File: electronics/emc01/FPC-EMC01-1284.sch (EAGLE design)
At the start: 74 parts, among them J1 USB-MINIB-5PIN, J11 CONN-RECT-16PIN-2ROW, J12 CONN-RECT-16PIN-2ROW, J13 CONN-RECT-16PIN-2ROW, J14 CONN-RECT-16PIN-2ROW, J15 DNP, J16 ICSP, J2 CONN-MOLEX-MICROFIT-6PIN, J3 DNP, J4A MOT-X, J5A MOT-Y, J6A MOT-Z, J7A CONN-RECT-3PINJST_PH_2MM, J8A CONN-RECT-3PINJST_PH_2MM, J9A CONN-RECT-3PINJST_PH_2MM, Q2 2N7002PW, U1 IC-ATMEGA1284P-AU, U2 FT231XS, X1 16Mhz

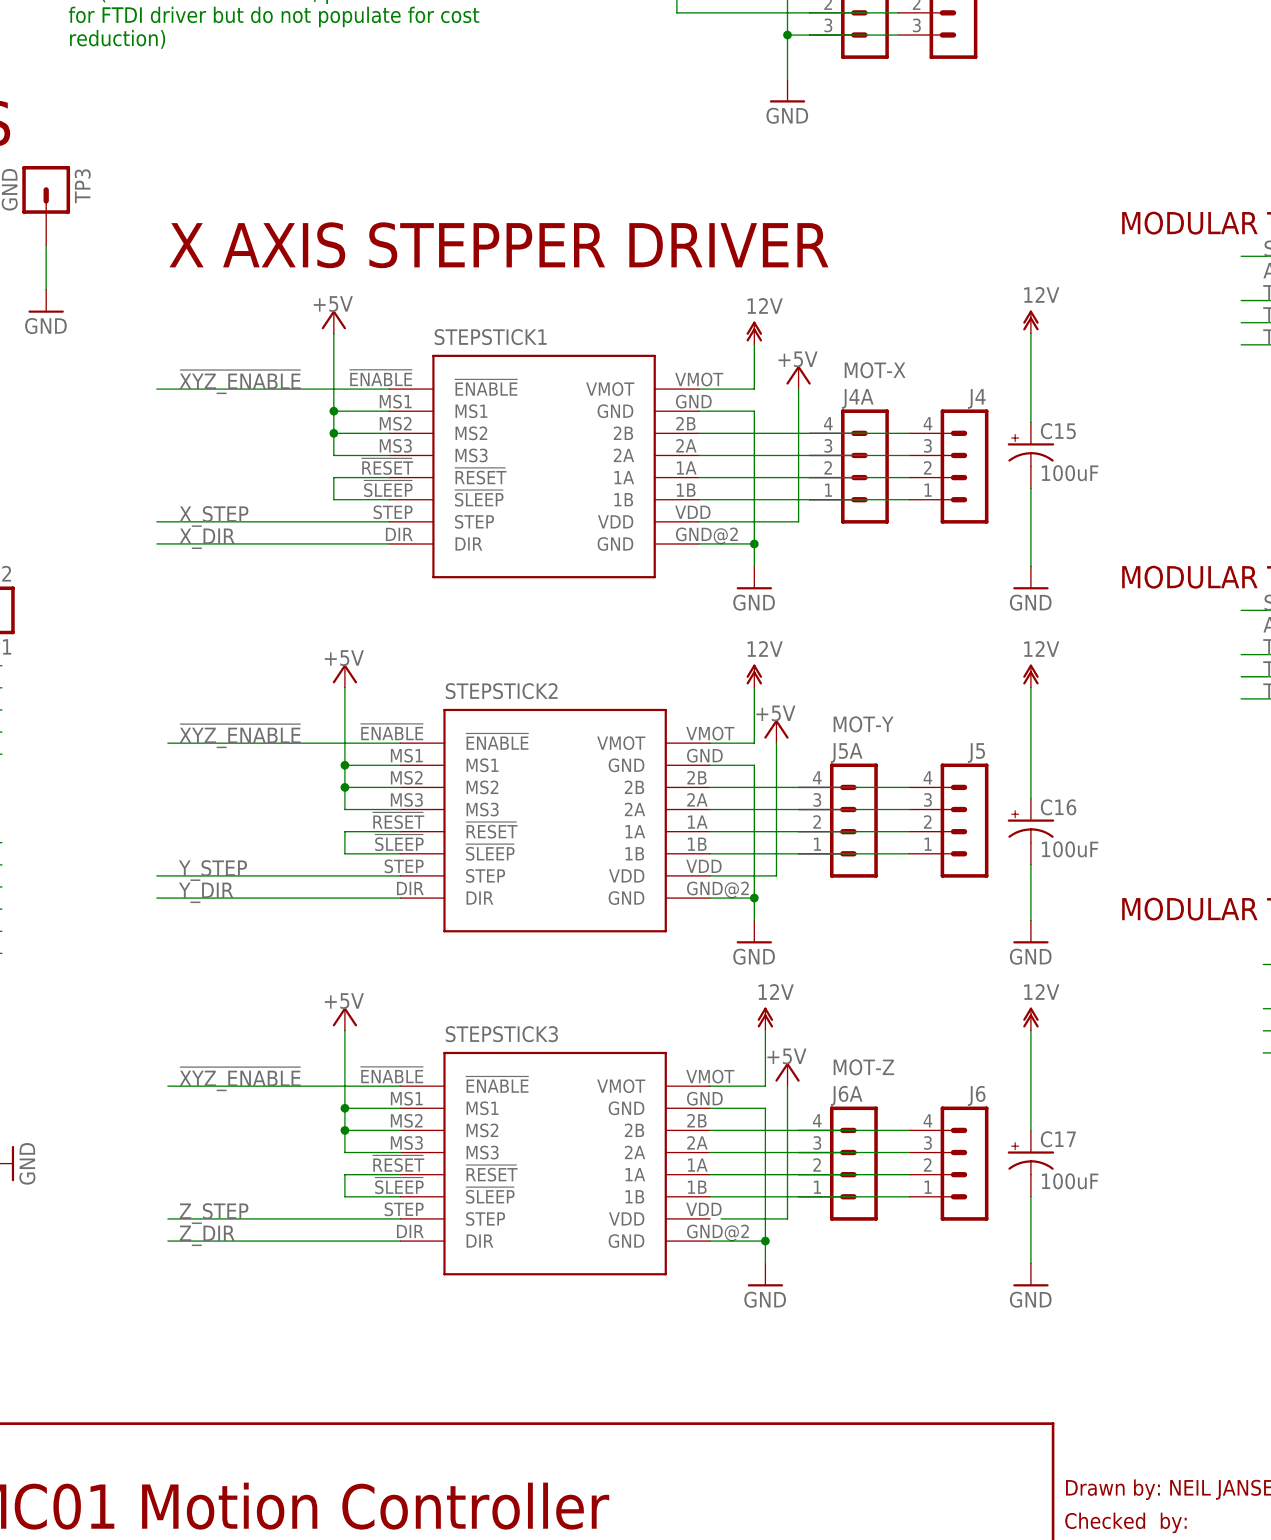
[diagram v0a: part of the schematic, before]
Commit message: Forgot some labels
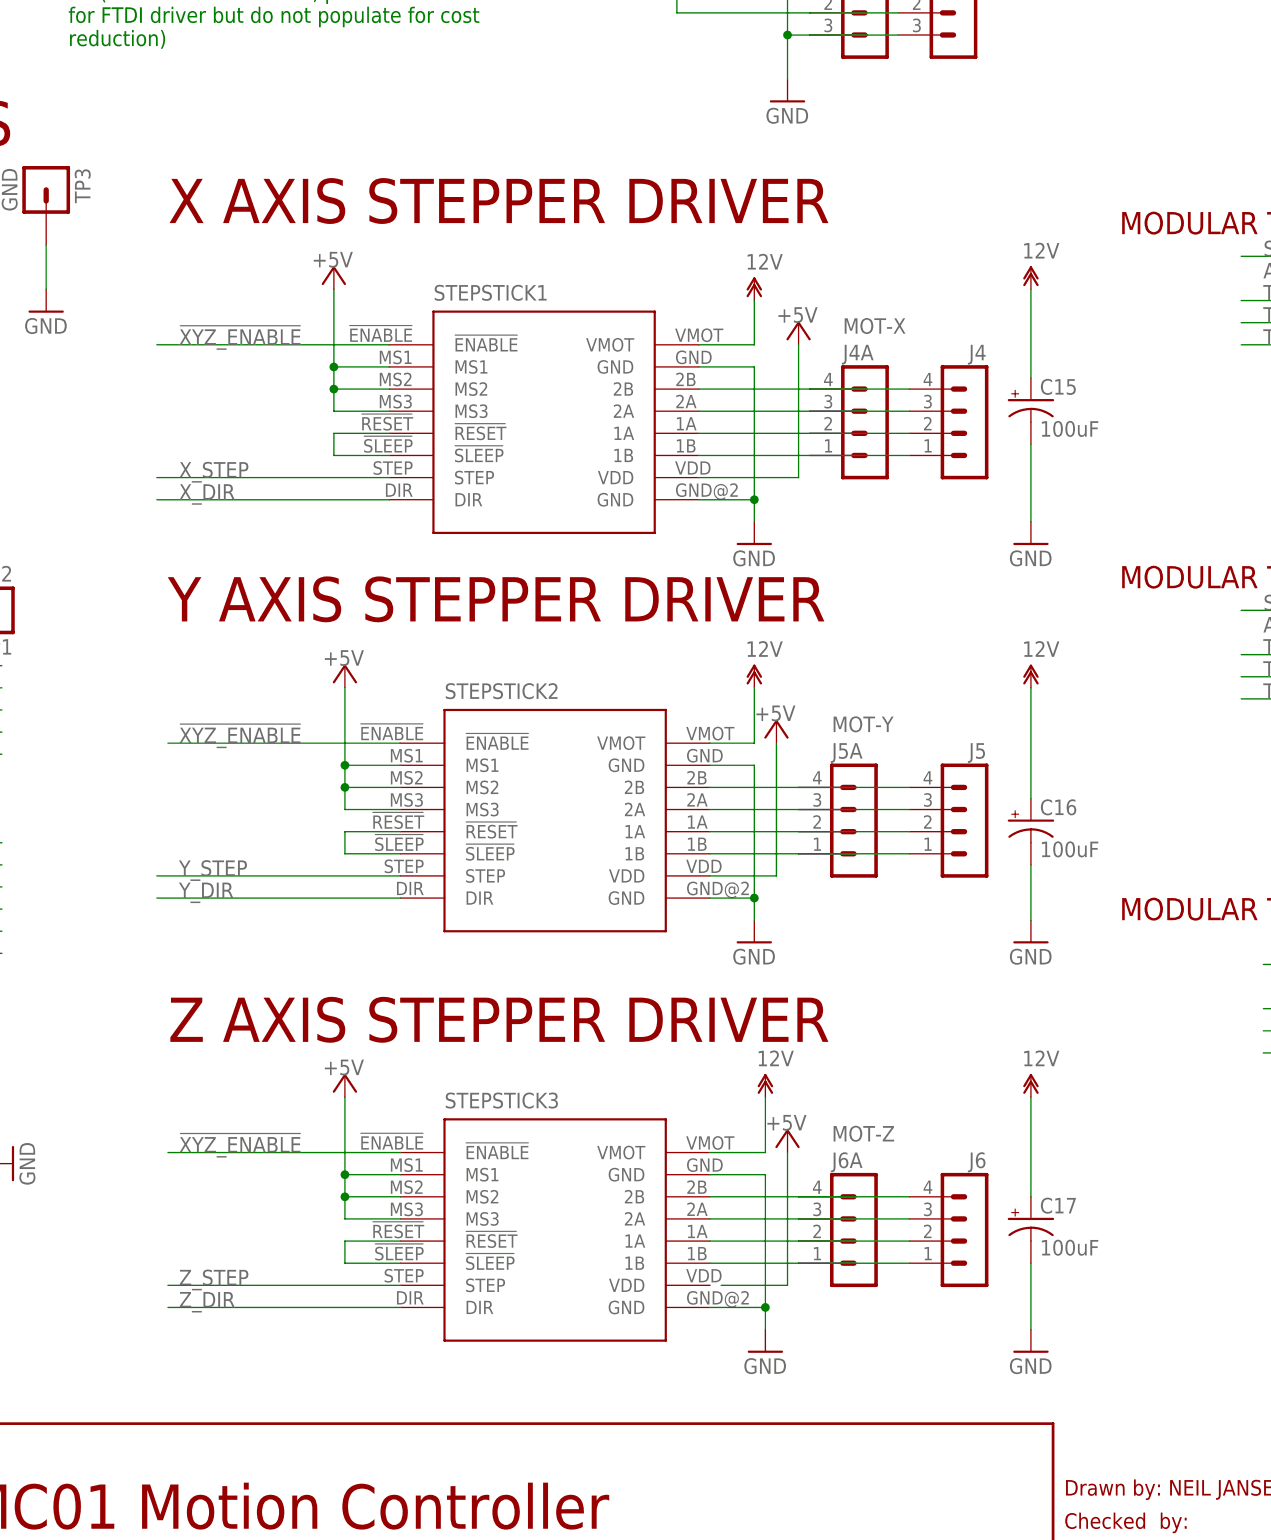
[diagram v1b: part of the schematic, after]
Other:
- note added: "Y AXIS STEPPER DRIVER"
- note added: "Z AXIS STEPPER DRIVER"
- moved on the sheet: C15, C17, J4, J4A, J6, J6A, STEPSTICK1, STEPSTICK3

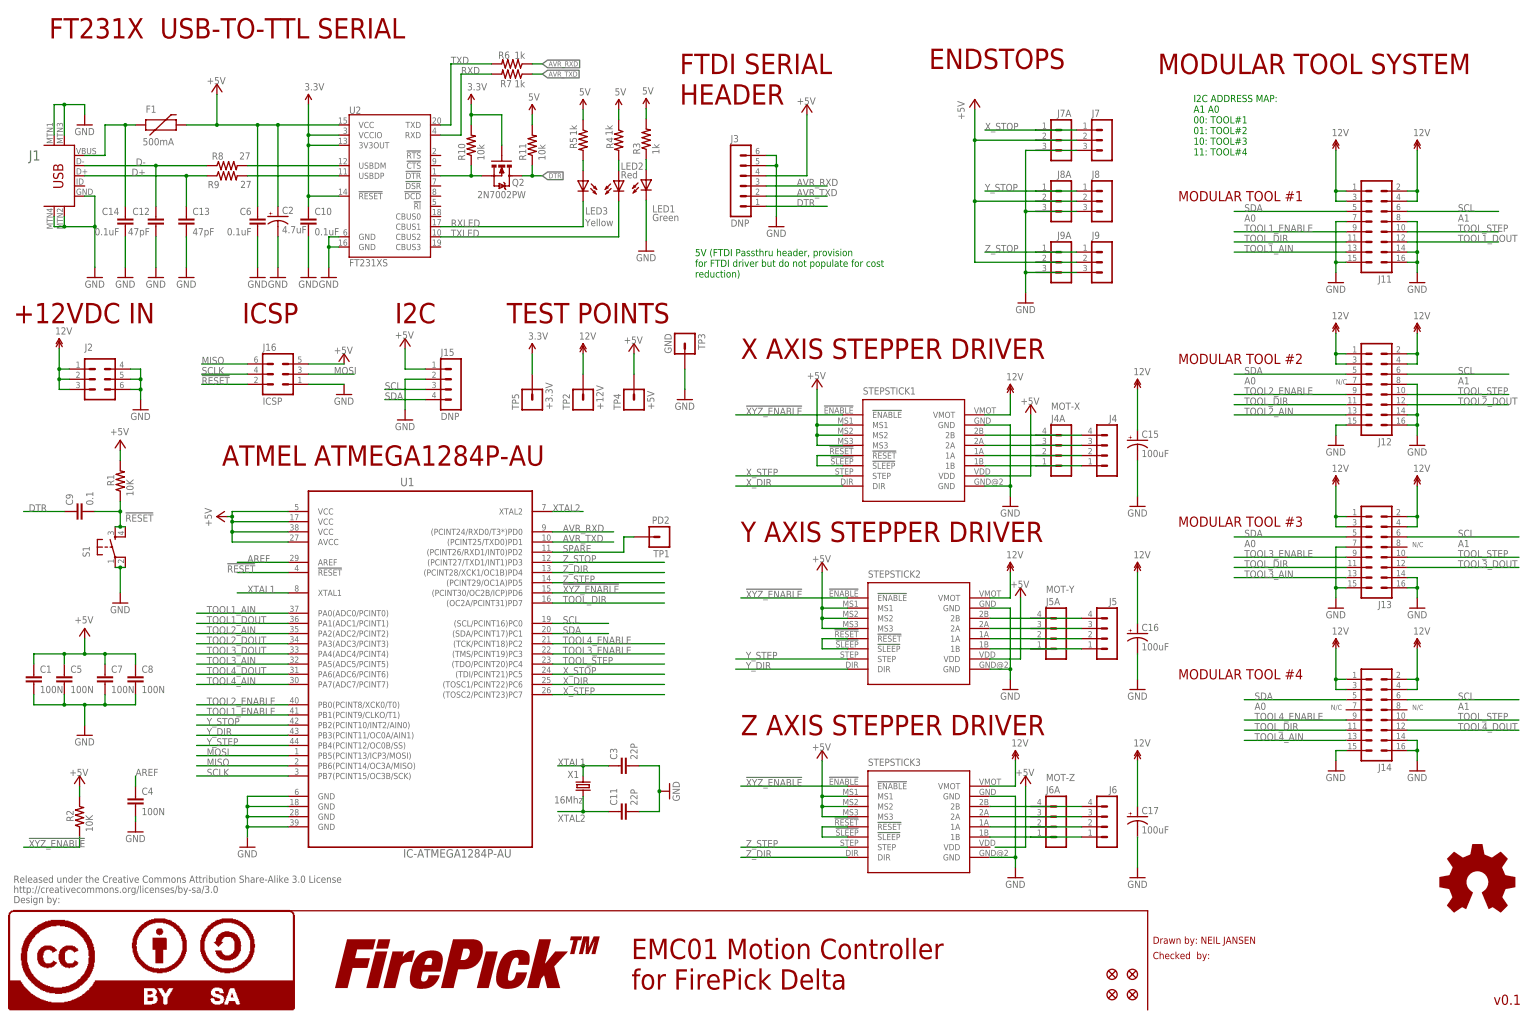
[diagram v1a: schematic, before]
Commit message: Fixed minor issues and changed modular tool connector pinout to allow better routing of GND and +12V planes
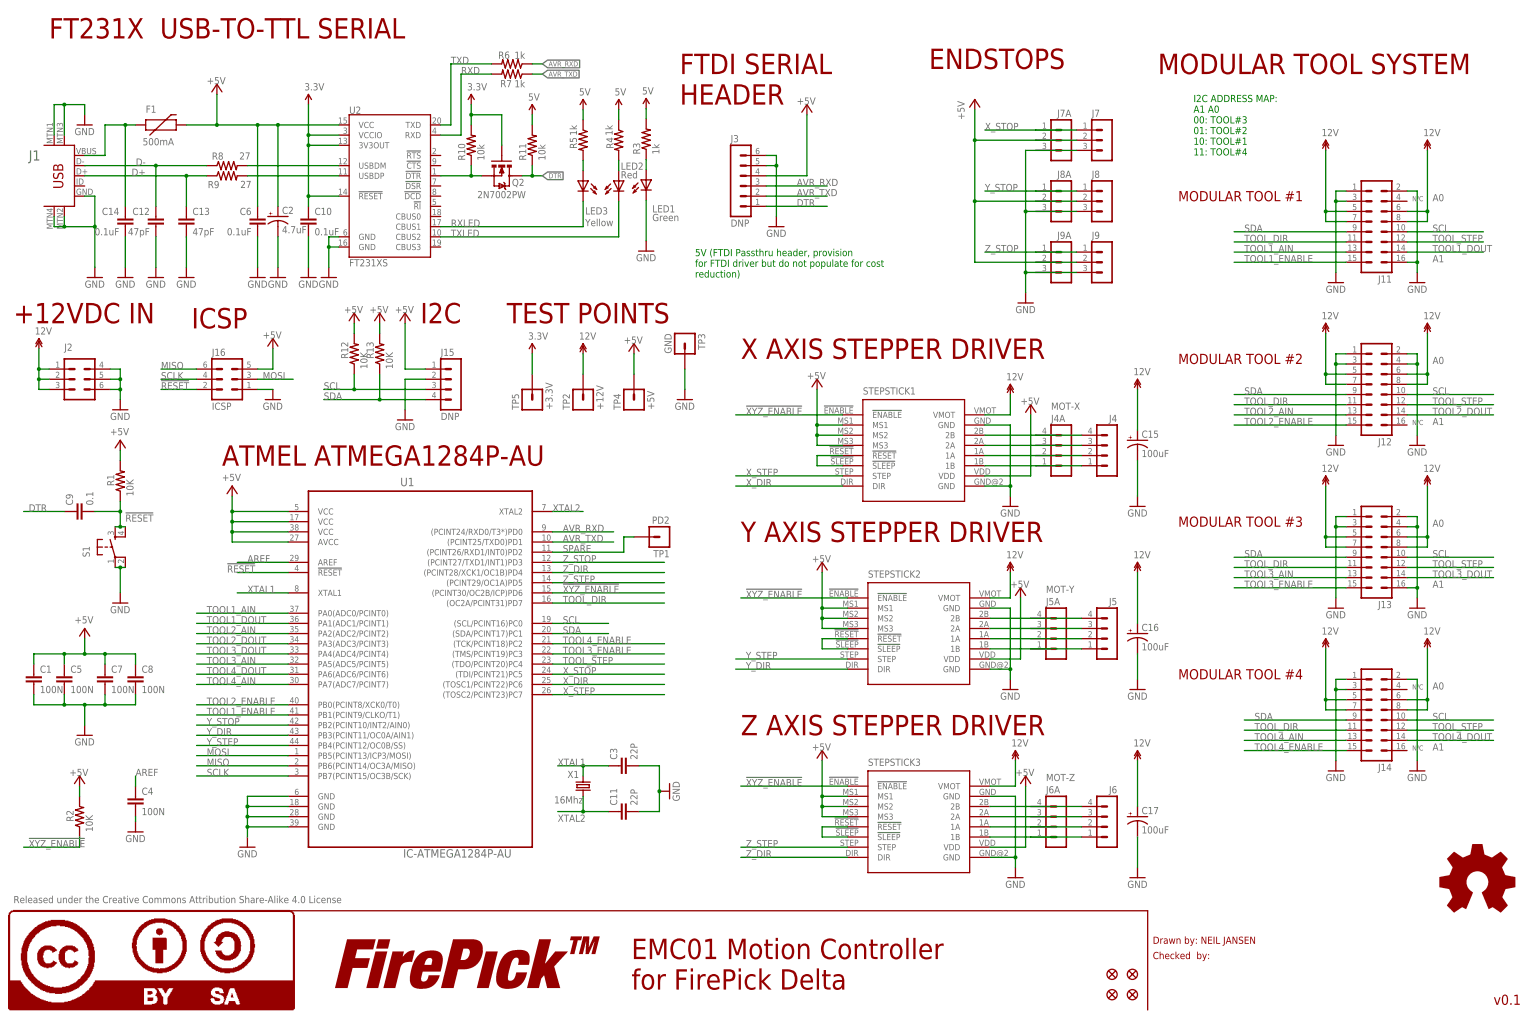
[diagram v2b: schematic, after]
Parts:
- removed U$15: CREATIVE_COMMONS, SparkFun:CREATIVE_COMMONS
- added R12, R13: 10K, SparkFun-Resistors:RESISTOR0805-RES
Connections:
- net +5V: now also R12.2, R13.2, STEPSTICK3.VDD
- net 12V: now also J11.5, J11.6, J11.7, J11.8, J12.5, J12.6, J12.7, J12.8, J13.5, J13.6, J13.7, J13.8, J14.5, J14.6, J14.7, J14.8; no longer J11.1, J11.2, J11.3, J11.4, J12.1, J12.2, J12.3, J12.4, J13.1, J13.2, J13.3, J13.4, J14.1, J14.2, J14.3, J14.4
- net GND: now also J11.1, J11.2, J11.3, J12.1, J12.2, J12.3, J12.4, J13.1, J13.2, J13.3, J13.4, J14.1, J14.2, J14.3; no longer J11.14, J11.15, J11.7, J11.8, J12.14, J12.15, J12.16, J12.8, J13.14, J13.15, J13.7, J14.14, J14.15, J14.16
- net SCL: now also J11.10, J12.10, J13.10, J14.10, R12.1; no longer J11.6, J12.6, J13.6, J14.6
- net SDA: now also J11.9, J12.9, J13.9, J14.9, R13.1; no longer J11.5, J12.5, J13.5, J14.5
- net TOOL1_DOUT: now also J11.14; no longer J11.12
- net TOOL1_ENABLE: now also J11.15; no longer J11.9
- net TOOL2_DOUT: now also J12.14; no longer J12.12
- net TOOL2_ENABLE: now also J12.15; no longer J12.9
- net TOOL3_DOUT: now also J13.14; no longer J13.12
- net TOOL3_ENABLE: now also J13.15; no longer J13.9
- net TOOL4_DOUT: now also J14.14; no longer J14.12
- net TOOL4_ENABLE: now also J14.15; no longer J14.9
- net TOOL_STEP: now also J11.12, J12.12, J13.12, J14.12; no longer J11.10, J12.10, J13.10, J14.10
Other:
- note added: "I2C ADDRESS MAP: A1 A0 00: TOOL#3 01: TOOL#2 10: TOOL#1 11: TOOL#4"
- note added: "Released under the Creative Commons Attribution Share-Alike 4.0 License"
- note removed: "I2C ADDRESS MAP: A1 A0 00: TOOL#1 01: TOOL#2 10: TOOL#3 11: TOOL#4"
- moved on the sheet: J16, J2
